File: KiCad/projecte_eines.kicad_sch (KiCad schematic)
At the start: 0 parts

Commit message: Canvis al diagrama de blocs, i subesquemes al kicad
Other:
- added sheet ETAPA1_POTENCIA (etapa1potencia.kicad_sch)
- added sheet ETAPA2_NOMETAPA2 (etapa2nometapa.kicad_sch)
- added sheet ETAPA3_SENSORS_I_CONTROL (etapa3sensorsicontrol.kicad_sch)
- added sheet ETAPA4_NOMETAPA4 (etapa4nometapa4.kicad_sch)
- note added: "15/03/2026"
- note added: "Combustible"
- note added: "ETAPA 2"
- note added: "ETAPA 4"
- note added: "POTÈNCIA"
- note added: "PROJECTE EINES DE DISSENY: COMBUSTIBLE"
- note added: "SENSORS I CONTROL"
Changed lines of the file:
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@@
 	(generator_version "9.0")
 	(paper "A4")
+	(text "PROJECTE EINES DE DISSENY: COMBUSTIBLE"
+		(exclude_from_sim no)
+		(at 230.632 173.99 0)
+		(effects
+			(font
+				(size 2.54 2.54)
+				(thickness 1.016)
+				(bold yes)
+			)
+		)
+	)
+	(text "POTÈNCIA"
+		(exclude_from_sim no)
+		(at 66.548 58.166 0)
+		(effects
+			(font
+				(size 5.08 5.08)
+				(thickness 0.635)
+			)
+		)
+	)
+	(text "SENSORS\nI\nCONTROL"
+		(exclude_from_sim no)
+		(at 67.564 125.476 0)
+		(effects
+			(font
+				(size 5.08 5.08)
+				(thickness 0.635)
+			)
+		)
+	)
+	(text "ETAPA 2"
+		(exclude_from_sim no)
+		(at 212.344 59.69 0)
+		(effects
+			(font
+				(size 5.08 5.08)
+				(thickness 0.635)
+			)
+		)
+	)
+	(text "ETAPA 4"
+		(exclude_from_sim no)
+		(at 214.63 124.714 0)
+		(effects
+			(font
+				(size 5.08 5.08)
+				(thickness 0.635)
+			)
+		)
+	)
+	(text "Combustible"
+		(exclude_from_sim no)
+		(at 192.786 189.992 0)
+		(effects
+			(font
+				(size 1.27 1.27)
+				(thickness 0.254)
+				(bold yes)
+			)
+		)
+	)
+	(text "15/03/2026"
+		(exclude_from_sim no)
+		(at 213.868 193.294 0)
+		(effects
+			(font
+				(size 1.27 1.27)
+				(thickness 0.254)
+				(bold yes)
+			)
+		)
+	)
+	(sheet
+		(at 30.48 33.02)
+		(size 76.2 53.34)
+		(exclude_from_sim no)
+		(in_bom yes)
+		(on_board yes)
+		(dnp no)
+		(fields_autoplaced yes)
+		(stroke
+			(width 0.1524)
+			(type solid)
+		)
+		(fill
+			(color 0 0 0 0.0000)
+		)
+		(property "Sheetname" "ETAPA1_POTENCIA"
+			(at 30.48 32.3084 0)
+			(effects
+				(font
+					(size 1.27 1.27)
+				)
+				(justify left bottom)
+			)
+		)
+		(property "Sheetfile" "etapa1potencia.kicad_sch"
+			(at 30.48 86.9446 0)
+			(effects
+				(font
+					(size 1.27 1.27)
+				)
+				(justify left top)
+			)
+		)
+		(instances
+			(project "projecte_eines"
+				(path "/c67ec3d5-698a-4d1a-92e9-687a1d354ef8"
+					(page "2")
+				)
+			)
+		)
+	)
+	(sheet
+		(at 29.21 96.52)
+		(size 76.2 53.34)
+		(exclude_from_sim no)
+		(in_bom yes)
+		(on_board yes)
+		(dnp no)
+		(fields_autoplaced yes)
+		(stroke
+			(width 0.1524)
+			(type solid)
+		)
+		(fill
+			(color 0 0 0 0.0000)
+		)
+		(property "Sheetname" "ETAPA3_SENSORS_I_CONTROL"
+			(at 29.21 95.8084 0)
+			(effects
+				(font
+					(size 1.27 1.27)
+				)
+				(justify left bottom)
+			)
+		)
+		(property "Sheetfile" "etapa3sensorsicontrol.kicad_sch"
+			(at 29.21 150.4446 0)
+			(effects
+				(font
+					(size 1.27 1.27)
+				)
+				(justify left top)
+			)
+		)
+		(instances
+			(project "projecte_eines"
+				(path "/c67ec3d5-698a-4d1a-92e9-687a1d354ef8"
+					(page "4")
+				)
+			)
+		)
+	)
+	(sheet
+		(at 173.99 96.52)
+		(size 76.2 53.34)
+		(exclude_from_sim no)
+		(in_bom yes)
+		(on_board yes)
+		(dnp no)
+		(fields_autoplaced yes)
+		(stroke
+			(width 0.1524)
+			(type solid)
+		)
+		(fill
+			(color 0 0 0 0.0000)
+		)
+		(property "Sheetname" "ETAPA4_NOMETAPA4"
+			(at 173.99 95.8084 0)
+			(effects
+				(font
+					(size 1.27 1.27)
+				)
+				(justify left bottom)
+			)
+		)
+		(property "Sheetfile" "etapa4nometapa4.kicad_sch"
+			(at 173.99 150.4446 0)
+			(effects
+				(font
+					(size 1.27 1.27)
+				)
+				(justify left top)
+			)
+		)
+		(instances
+			(project "projecte_eines"
+				(path "/c67ec3d5-698a-4d1a-92e9-687a1d354ef8"
+					(page "5")
+				)
+			)
+		)
+	)
+	(sheet
+		(at 173.99 33.02)
+		(size 76.2 53.34)
+		(exclude_from_sim no)
+		(in_bom yes)
+		(on_board yes)
+		(dnp no)
+		(fields_autoplaced yes)
+		(stroke
+			(width 0.1524)
+			(type solid)
+		)
+		(fill
+			(color 0 0 0 0.0000)
+		)
+		(property "Sheetname" "ETAPA2_NOMETAPA2"
+			(at 173.99 32.3084 0)
+			(effects
+				(font
+					(size 1.27 1.27)
+				)
+				(justify left bottom)
+			)
+		)
+		(property "Sheetfile" "etapa2nometapa.kicad_sch"
+			(at 173.99 86.9446 0)
+			(effects
+				(font
+					(size 1.27 1.27)
+				)
+				(justify left top)
+			)
+		)
+		(instances
+			(project "projecte_eines"
+				(path "/c67ec3d5-698a-4d1a-92e9-687a1d354ef8"
+					(page "3")
+				)
+			)
+		)
+	)
 	(sheet_instances
 		(path "/"

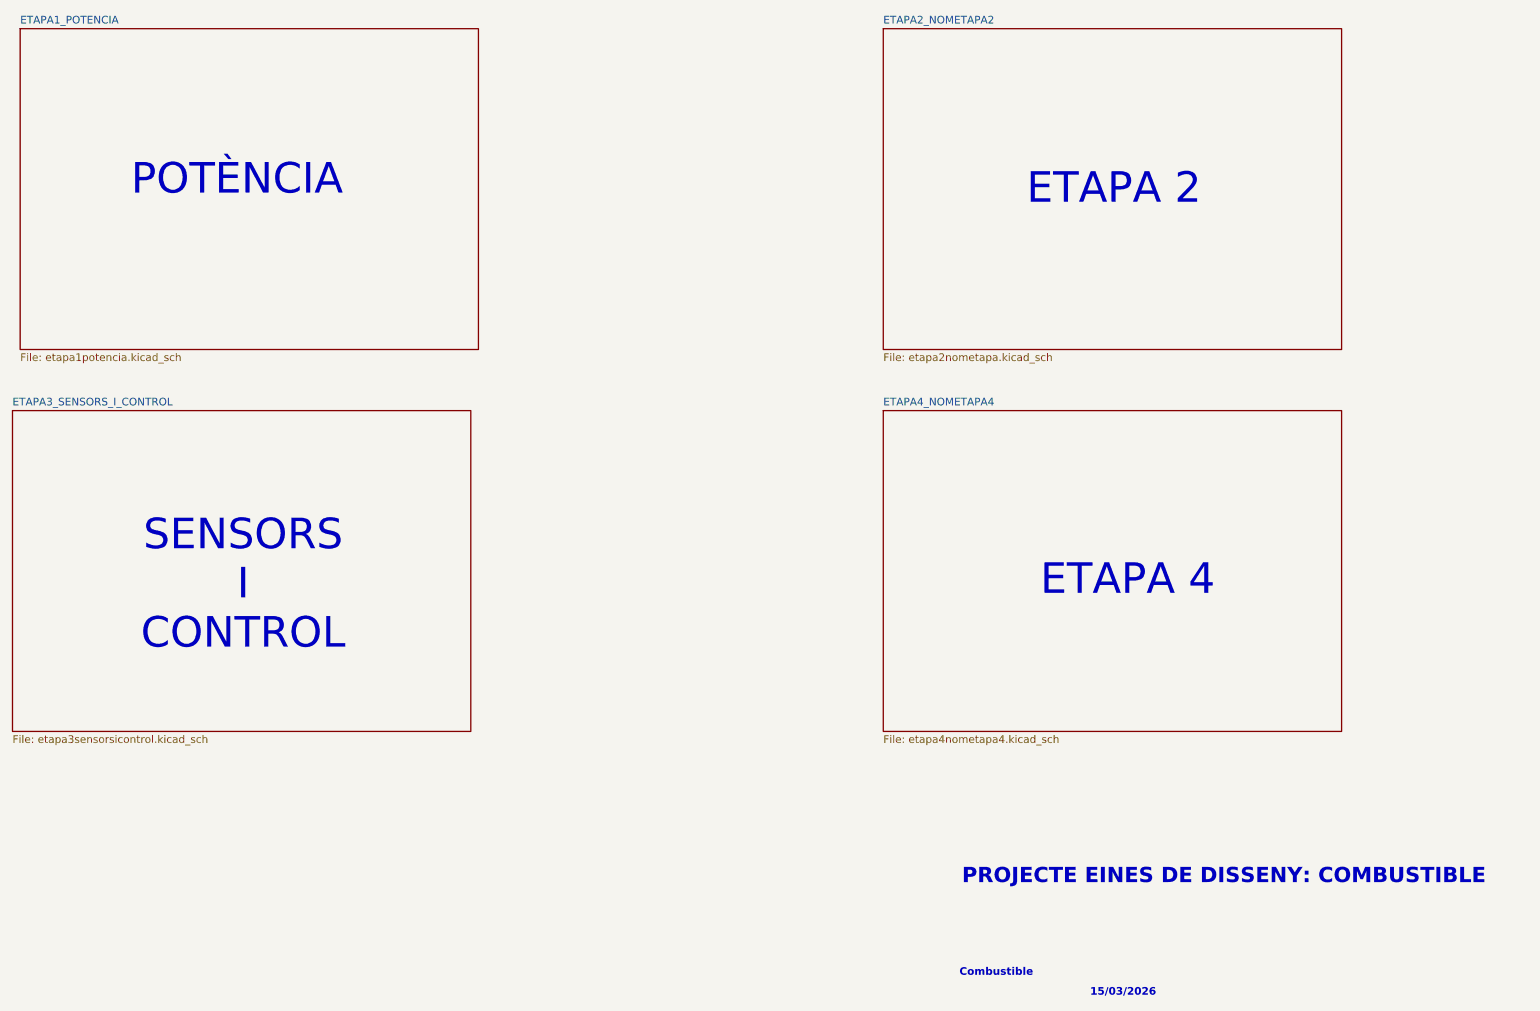
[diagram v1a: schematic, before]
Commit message: Canvis del probelam de l'esquematic
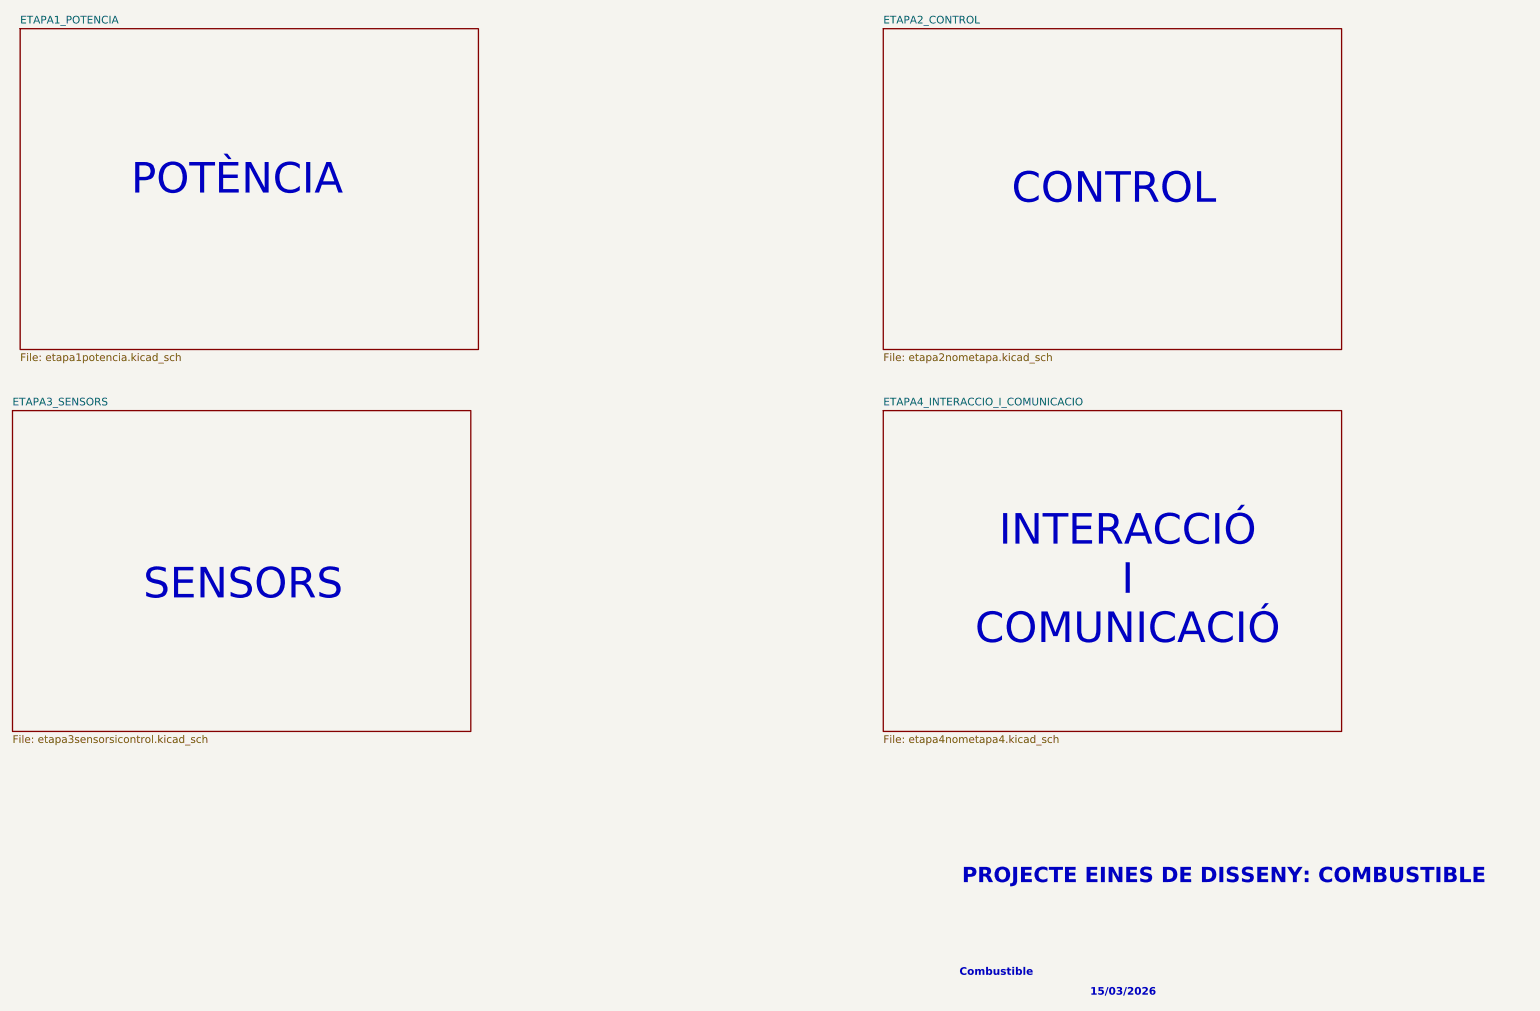
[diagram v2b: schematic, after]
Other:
- sheet ETAPA2_NOMETAPA2 renamed ETAPA2_CONTROL
- sheet ETAPA3_SENSORS_I_CONTROL renamed ETAPA3_SENSORS
- sheet ETAPA4_NOMETAPA4 renamed ETAPA4_INTERACCIO_I_COMUNICACIO
- note added: "CONTROL"
- note added: "INTERACCIÓ I COMUNICACIÓ"
- note added: "SENSORS"
- note removed: "ETAPA 2"
- note removed: "ETAPA 4"
- note removed: "SENSORS I CONTROL"
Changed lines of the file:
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@@
 		)
 	)
-	(text "SENSORS\nI\nCONTROL"
+	(text "SENSORS\n"
 		(exclude_from_sim no)
 		(at 67.564 125.476 0)
@@
 		)
 	)
-	(text "ETAPA 2"
+	(text "CONTROL"
 		(exclude_from_sim no)
 		(at 212.344 59.69 0)
@@
 		)
 	)
-	(text "ETAPA 4"
+	(text "INTERACCIÓ\nI\nCOMUNICACIÓ"
 		(exclude_from_sim no)
 		(at 214.63 124.714 0)
@@
 			(color 0 0 0 0.0000)
 		)
-		(property "Sheetname" "ETAPA3_SENSORS_I_CONTROL"
+		(property "Sheetname" "ETAPA3_SENSORS"
 			(at 29.21 95.8084 0)
 			(effects
@@
 			(color 0 0 0 0.0000)
 		)
-		(property "Sheetname" "ETAPA4_NOMETAPA4"
+		(property "Sheetname" "ETAPA4_INTERACCIO_I_COMUNICACIO"
 			(at 173.99 95.8084 0)
 			(effects
@@
 			(color 0 0 0 0.0000)
 		)
-		(property "Sheetname" "ETAPA2_NOMETAPA2"
+		(property "Sheetname" "ETAPA2_CONTROL"
 			(at 173.99 32.3084 0)
 			(effects
